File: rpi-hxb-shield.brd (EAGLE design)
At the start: 20 x 35 mm, 30 parts, among them Q1 CRYSTALX22, U2 24LC128-I/SN

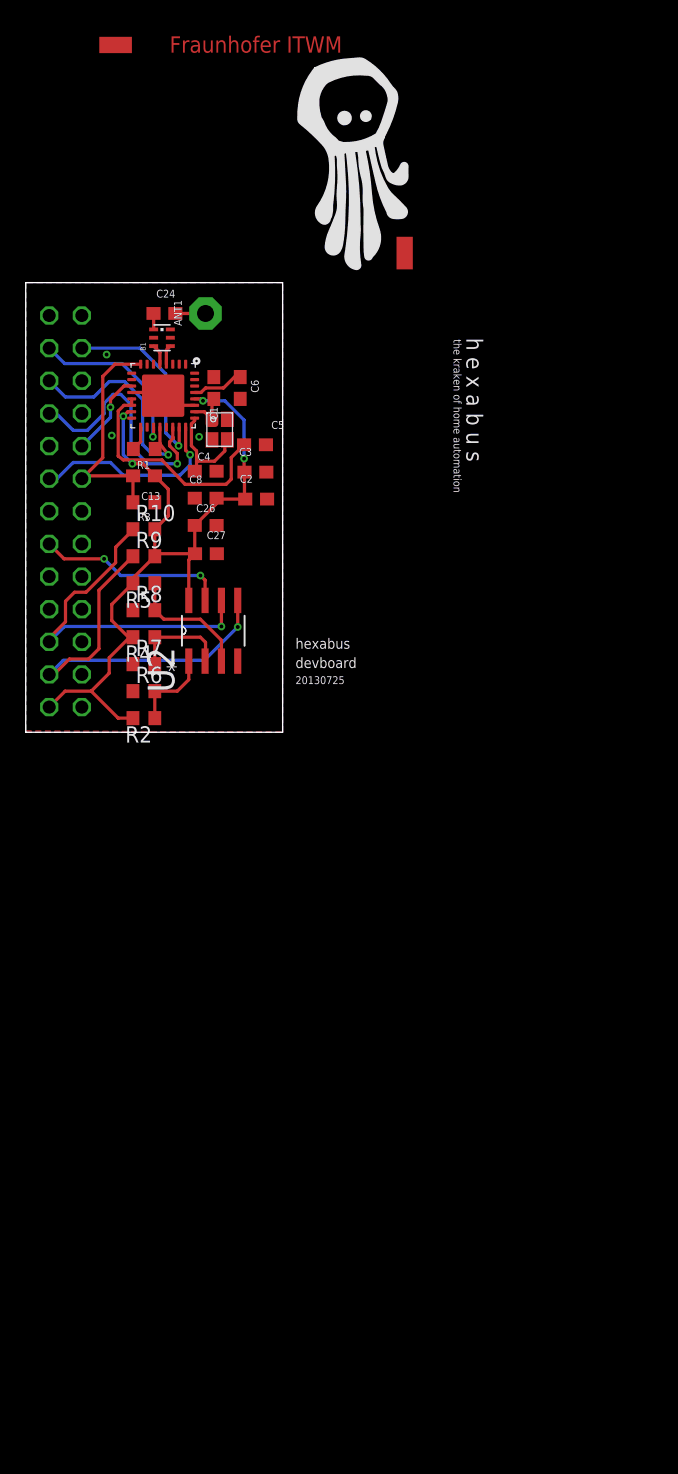
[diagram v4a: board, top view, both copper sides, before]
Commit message: sketch of new layout for accomodation the antenna on the pcb
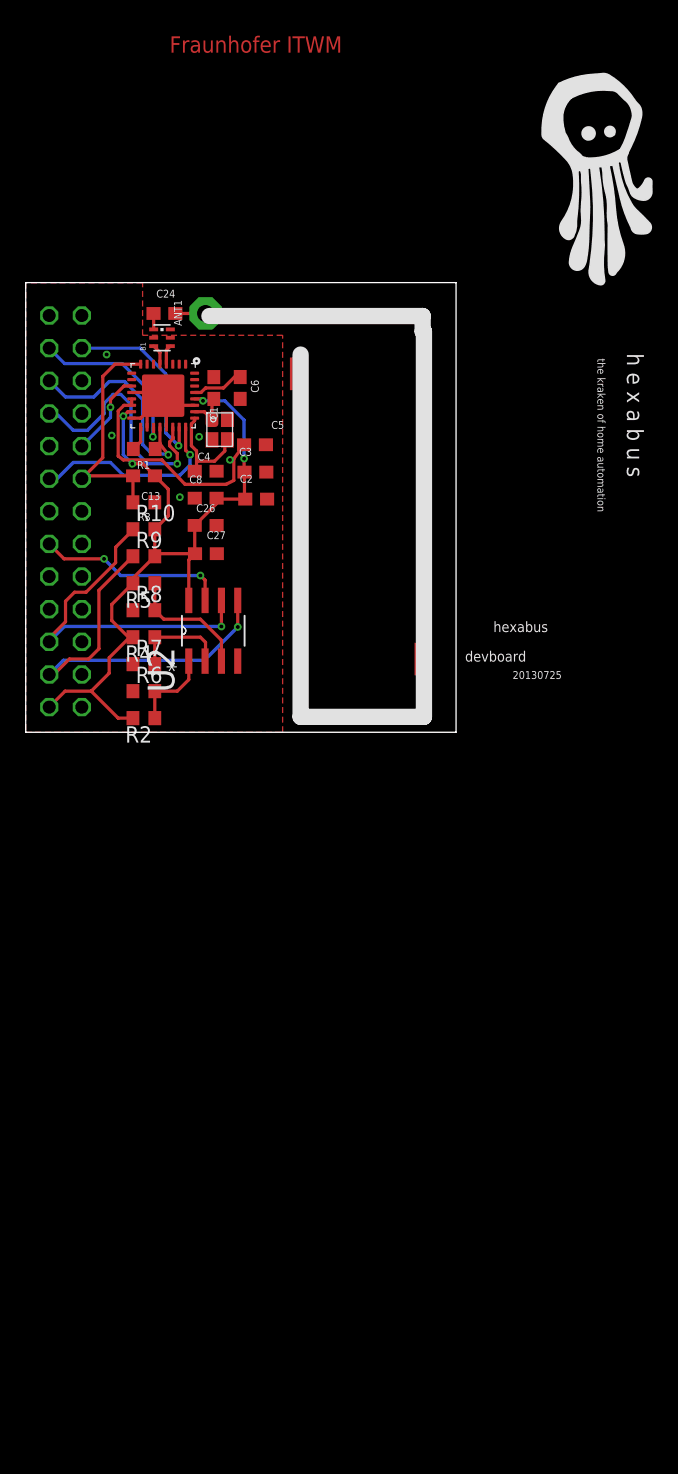
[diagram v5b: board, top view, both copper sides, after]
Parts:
- moved PAD2 31.6 mm to (30.9, 5.70)
- moved PAD1 29.3 mm to (21.2, 27.9), turned to 180 degrees
- moved U$1 19.0 mm to (40.2, 34.9)
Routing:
- net GND: track 5.31 -> 11.7 mm, vias 3 -> 5
- removed copper zone on layer 16, net GND
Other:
- board size 20 x 35 mm -> 33.5 x 35 mm
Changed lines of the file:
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@@
 <layer number="23" name="tOrigins" color="15" fill="1" visible="yes" active="yes"/>
 <layer number="24" name="bOrigins" color="15" fill="1" visible="yes" active="yes"/>
-<layer number="25" name="tNames" color="7" fill="1" visible="yes" active="yes"/>
+<layer number="25" name="tNames" color="7" fill="1" visible="no" active="yes"/>
 <layer number="26" name="bNames" color="7" fill="1" visible="yes" active="yes"/>
-<layer number="27" name="tValues" color="7" fill="1" visible="yes" active="yes"/>
+<layer number="27" name="tValues" color="7" fill="1" visible="no" active="yes"/>
 <layer number="28" name="bValues" color="7" fill="1" visible="yes" active="yes"/>
 <layer number="29" name="tStop" color="7" fill="3" visible="no" active="yes"/>
@@
 <board>
 <plain>
-<wire x1="0" y1="0" x2="20" y2="0" width="0" layer="20"/>
-<wire x1="20" y1="0" x2="20" y2="35" width="0" layer="20"/>
-<wire x1="20" y1="35" x2="0" y2="35" width="0" layer="20"/>
+<wire x1="0" y1="0" x2="33.5" y2="0" width="0" layer="20"/>
+<wire x1="33.5" y1="0" x2="33.5" y2="35" width="0" layer="20"/>
+<wire x1="33.5" y1="35" x2="0" y2="35" width="0" layer="20"/>
 <wire x1="0" y1="35" x2="0" y2="0" width="0" layer="20"/>
-<text x="34.3" y="30.7" size="1.27" layer="21" font="vector" ratio="15" rot="SR270">h e x a b u s</text>
+<text x="46.8" y="29.5" size="1.27" layer="21" font="vector" ratio="15" rot="SR270">h e x a b u s</text>
 <text x="11.2" y="52.9" size="1.27" layer="1" font="vector" ratio="12">Fraunhofer ITWM</text>
-<text x="33.3" y="30.6" size="0.6096" layer="21" font="vector" distance="100" rot="SR270">the kraken of home automation</text>
-<text x="21" y="6.5" size="0.8128" layer="21" font="vector" ratio="12">hexabus</text>
-<text x="21" y="5" size="0.8128" layer="21" font="vector">devboard</text>
-<text x="21" y="3.75" size="0.6096" layer="21" font="vector">20130725</text>
+<text x="44.5" y="29.1" size="0.6096" layer="21" font="vector" distance="100" rot="SR270">the kraken of home automation</text>
+<text x="36.4" y="7.8" size="0.8128" layer="21" font="vector" ratio="12">hexabus</text>
+<text x="34.2" y="5.5" size="0.8128" layer="21" font="vector">devboard</text>
+<text x="37.9" y="4.15" size="0.6096" layer="21" font="vector">20130725</text>
+<wire x1="14.3" y1="32.4" x2="30.9" y2="32.4" width="1.27" layer="21"/>
+<wire x1="30.9" y1="32.4" x2="30.9" y2="31.2" width="1.27" layer="21"/>
+<wire x1="30.9" y1="31.2" x2="31" y2="31.2" width="1.27" layer="21"/>
+<wire x1="31" y1="31.2" x2="31" y2="1.2" width="1.27" layer="21"/>
+<wire x1="31" y1="1.2" x2="21.4" y2="1.2" width="1.27" layer="21"/>
+<wire x1="21.4" y1="1.2" x2="21.4" y2="29.4" width="1.27" layer="21"/>
 </plain>
 <attributes>
@@
 <attribute name="NAME" x="13.375" y="21.155" size="0.6096" layer="25"/>
 </element>
-<element name="PAD1" library="wirepad" package="SMD1,27-2,54" value="" x="7" y="53.5" smashed="yes" rot="R90">
-<attribute name="VALUE" x="7" y="53.5" size="0.0254" layer="27" rot="R90"/>
-</element>
-<element name="PAD2" library="wirepad" package="SMD1,27-2,54" value="" x="29.5" y="37.3" smashed="yes">
-<attribute name="VALUE" x="29.5" y="37.3" size="0.0254" layer="27"/>
-</element>
-<element name="U$1" library="artwork" package="HEXAKRAKE" value="HEXAKRAKE" x="21.2" y="36.1"/>
+<element name="PAD1" library="wirepad" package="SMD1,27-2,54" value="" x="21.2" y="27.9" smashed="yes" rot="R180">
+<attribute name="VALUE" x="21.2" y="27.9" size="0.0254" layer="27" rot="R180"/>
+</element>
+<element name="PAD2" library="wirepad" package="SMD1,27-2,54" value="" x="30.9" y="5.7" smashed="yes">
+<attribute name="VALUE" x="30.9" y="5.7" size="0.0254" layer="27"/>
+</element>
+<element name="U$1" library="artwork" package="HEXAKRAKE" value="HEXAKRAKE" x="40.2" y="34.9"/>
 <element name="U2" library="hexabus" package="SOIC127P600X175-8N" value="24LC128-I/SN" x="14.6" y="7.9" rot="R90">
 <attribute name="PACKAGE" value="SOIC-8" x="14.6" y="7.9" size="1.778" layer="27" rot="R90" display="off"/>
@@
 <contactref element="JP1" pad="14"/>
 <contactref element="JP1" pad="20"/>
-<polygon width="0.254" layer="16" spacing="0.254">
-<vertex x="0" y="0"/>
-<vertex x="20" y="0"/>
-<vertex x="20" y="35"/>
-<vertex x="0" y="35"/>
-</polygon>
-<polygon width="0.254" layer="1" spacing="0.254">
-<vertex x="0" y="0.1"/>
-<vertex x="20" y="0"/>
-<vertex x="20" y="35"/>
-<vertex x="0" y="35"/>
-</polygon>
 <via x="6.7" y="23.1" extent="1-16" drill="0.3"/>
 <via x="6.3" y="29.4" extent="1-16" drill="0.3"/>
 <wire x1="8.25" y1="26.45" x2="10.45" y2="26.45" width="0.254" layer="1"/>
 <wire x1="10.45" y1="26.45" x2="10.7" y2="26.2" width="0.254" layer="1"/>
-<wire x1="13.15" y1="25.45" x2="11.45" y2="25.45" width="0.254" layer="1"/>
-<wire x1="11.45" y1="25.45" x2="10.7" y2="26.2" width="0.254" layer="1"/>
 <via x="13.5" y="23" extent="1-16" drill="0.3"/>
-<wire x1="14.5" y1="22.76" x2="14.86" y2="20.32" width="0" layer="19" extent="1-1"/>
+<wire x1="8.25" y1="24.45" x2="8.95" y2="24.45" width="0.254" layer="1"/>
+<wire x1="8.95" y1="24.45" x2="9.45" y2="24.95" width="0.254" layer="1"/>
+<wire x1="9.45" y1="23.75" x2="9.45" y2="24.95" width="0.254" layer="1"/>
+<wire x1="9.45" y1="24.95" x2="10.7" y2="26.2" width="0.254" layer="1"/>
+<wire x1="10.95" y1="23.75" x2="10.95" y2="25.6" width="0.254" layer="1"/>
+<wire x1="10.95" y1="25.6" x2="10.95" y2="25.95" width="0.254" layer="1"/>
+<wire x1="10.95" y1="25.95" x2="10.7" y2="26.2" width="0.254" layer="1"/>
+<via x="15.9" y="21.2" extent="1-16" drill="0.3"/>
+<via x="12" y="18.3" extent="1-16" drill="0.3"/>
+<wire x1="13.15" y1="25.45" x2="11.1" y2="25.45" width="0.254" layer="1"/>
+<wire x1="11.1" y1="25.45" x2="10.95" y2="25.6" width="0.254" layer="1"/>
+<polygon width="0.254" layer="1">
+<vertex x="0" y="0"/>
+<vertex x="20" y="0"/>
+<vertex x="20" y="30.9"/>
+<vertex x="9.1" y="30.9"/>
+<vertex x="9.1" y="35"/>
+<vertex x="0" y="35"/>
+</polygon>
+<wire x1="11.2602" y1="30.7086" x2="11.2602" y2="31.3586" width="0" layer="19" extent="1-1"/>
 <wire x1="13.15" y1="25.45" x2="13.15" y2="26.95" width="0" layer="19" extent="1-1"/>
-<wire x1="10.95" y1="23.75" x2="11.45" y2="25.45" width="0" layer="19" extent="1-1"/>
-<wire x1="9.45" y1="23.75" x2="10.95" y2="23.75" width="0" layer="19" extent="1-1"/>
-<wire x1="8.25" y1="24.45" x2="9.45" y2="23.75" width="0" layer="19" extent="1-1"/>
+<wire x1="12" y1="18.3" x2="10.05" y2="17.9" width="0" layer="19" extent="1-1"/>
+<wire x1="14.5" y1="22.76" x2="15.7" y2="24.36" width="0" layer="19" extent="1-1"/>
 <wire x1="6.7" y1="23.1" x2="8.25" y2="24.45" width="0" layer="19" extent="1-1"/>
-<wire x1="13.16" y1="18.22" x2="14.86" y2="20.32" width="0" layer="19" extent="1-1"/>
+<wire x1="15.9" y1="21.2" x2="14.5" y2="22.76" width="0" layer="19" extent="1-1"/>
 </signal>
 <signal name="IRQ">
@@
 <wire x1="10.6" y1="21.2" x2="12.4" y2="19.3" width="0.254" layer="1"/>
 <wire x1="12.4" y1="19.3" x2="15.6" y2="19.3" width="0.254" layer="1"/>
-<wire x1="15.6" y1="19.3" x2="16" y2="19.7" width="0.254" layer="1"/>
-<wire x1="16" y1="19.7" x2="16" y2="21.38" width="0.254" layer="1"/>
-<wire x1="16" y1="21.38" x2="17" y2="22.38" width="0.254" layer="1"/>
+<wire x1="15.6" y1="19.3" x2="16.2" y2="19.6" width="0.254" layer="1"/>
+<wire x1="16.2" y1="19.6" x2="16.2" y2="21.28" width="0.254" layer="1"/>
+<wire x1="16.2" y1="21.28" x2="17" y2="22.38" width="0.254" layer="1"/>
 <wire x1="8.25" y1="25.45" x2="8.25" y2="25.95" width="0.254" layer="1"/>
 </signal>

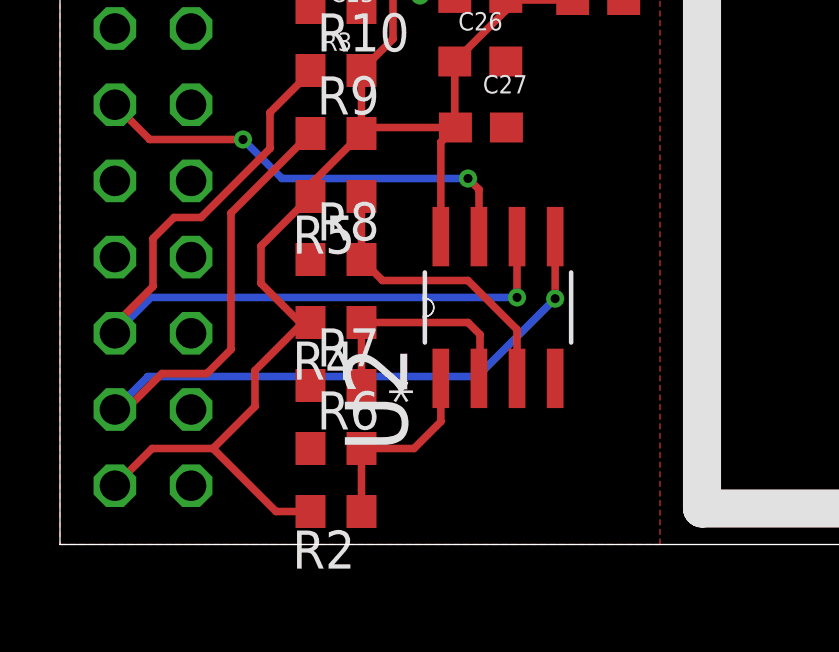
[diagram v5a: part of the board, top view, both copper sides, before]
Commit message: EEPOM now with fixed address (hardwired)
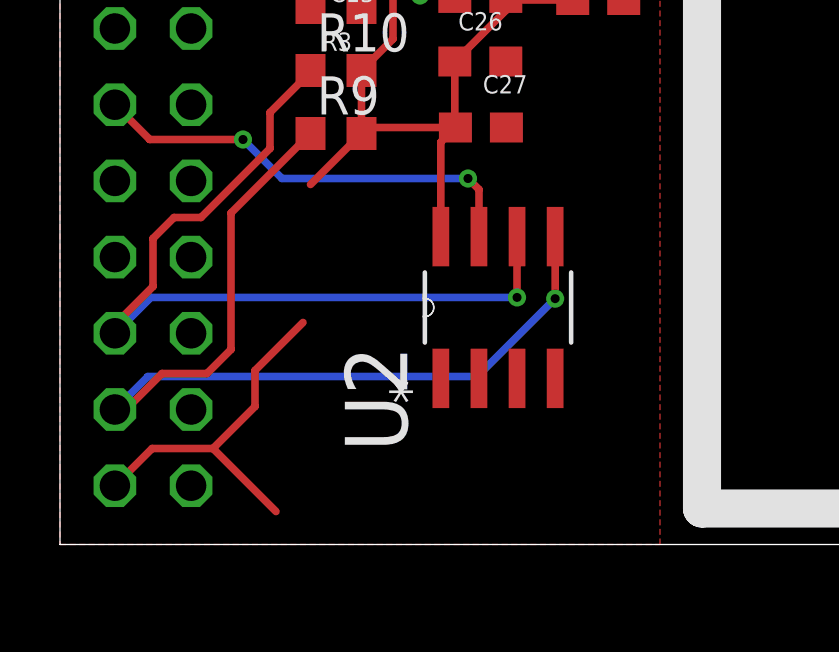
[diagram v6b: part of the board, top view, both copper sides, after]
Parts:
- removed R2, R4, R5, R6, R7, R8: 0R, rcl:R0603
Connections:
- removed net N$10: R5.1, R8.2, U2.3
- removed net N$4: R2.1, R6.2, U2.1
- removed net N$9: R4.1, R7.2, U2.2
- net GND: now also U2.1, U2.2, U2.3; no longer R6.1, R7.1, R8.1
- net VCC: no longer R2.2, R4.2, R5.2
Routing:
- net N$10: track 9.88 -> 0.00 mm
- net N$9: track 7.69 -> 0.00 mm
- net VCC: track 61.3 -> 53.7 mm
- net N$4: track 6.56 -> 0.00 mm
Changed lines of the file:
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@@
 <attribute name="OC_FARNELL" value="9757937" x="14.6" y="7.9" size="1.778" layer="27" rot="R90" display="off"/>
 </element>
-<element name="R2" library="rcl" package="R0603" value="0R" x="9.2" y="1.1" rot="R180"/>
-<element name="R4" library="rcl" package="R0603" value="0R" x="9.2" y="7.4" rot="R180"/>
-<element name="R5" library="rcl" package="R0603" value="0R" x="9.2" y="11.6" rot="R180"/>
-<element name="R6" library="rcl" package="R0603" value="0R" x="9.2" y="3.2"/>
-<element name="R7" library="rcl" package="R0603" value="0R" x="9.2" y="5.3"/>
-<element name="R8" library="rcl" package="R0603" value="0R" x="9.2" y="9.5"/>
 <element name="JP1" library="pinhead" package="2X13" value="" x="3.1" y="17.2" rot="MR90"/>
 <element name="R9" library="rcl" package="R0603" value="4k7" x="9.2" y="13.7"/>
@@
 <contactref element="U1" pad="33"/>
 <contactref element="U2" pad="4"/>
-<contactref element="R8" pad="1"/>
-<contactref element="R7" pad="1"/>
-<contactref element="R6" pad="1"/>
 <contactref element="JP1" pad="25"/>
 <contactref element="JP1" pad="9"/>
@@
 <vertex x="0" y="35"/>
 </polygon>
+<contactref element="U2" pad="3"/>
+<contactref element="U2" pad="2"/>
+<contactref element="U2" pad="1"/>
 <wire x1="11.2602" y1="30.7086" x2="11.2602" y2="31.3586" width="0" layer="19" extent="1-1"/>
+<wire x1="15.235" y1="5.5378" x2="16.505" y2="5.5378" width="0" layer="19" extent="1-1"/>
+<wire x1="13.965" y1="5.5378" x2="15.235" y2="5.5378" width="0" layer="19" extent="1-1"/>
+<wire x1="12.695" y1="5.5378" x2="13.965" y2="5.5378" width="0" layer="19" extent="1-1"/>
 <wire x1="13.15" y1="25.45" x2="13.15" y2="26.95" width="0" layer="19" extent="1-1"/>
 <wire x1="12" y1="18.3" x2="10.05" y2="17.9" width="0" layer="19" extent="1-1"/>
@@
 <contactref element="U2" pad="8"/>
 <contactref element="U2" pad="8"/>
-<contactref element="R5" pad="2"/>
-<contactref element="R4" pad="2"/>
-<contactref element="R2" pad="2"/>
 <contactref element="JP1" pad="1"/>
 <contactref element="R9" pad="2"/>
@@
 <wire x1="1.83" y1="1.96" x2="3.07" y2="3.2" width="0.254" layer="1"/>
 <wire x1="3.07" y1="3.2" x2="5.1" y2="3.2" width="0.254" layer="1"/>
-<wire x1="8.35" y1="1.1" x2="7.2" y2="1.1" width="0.254" layer="1"/>
 <wire x1="7.2" y1="1.1" x2="5.1" y2="3.2" width="0.254" layer="1"/>
 <wire x1="13.18" y1="13.9" x2="12.695" y2="13.415" width="0.254" layer="1"/>
@@
 <wire x1="11.1" y1="16.85" x2="11.1" y2="18.92" width="0.254" layer="1"/>
 <wire x1="11.1" y1="18.92" x2="10.06" y2="19.96" width="0.254" layer="1"/>
-<wire x1="8.35" y1="7.4" x2="8.1" y2="7.4" width="0.254" layer="1"/>
 <wire x1="8.1" y1="7.4" x2="6.5" y2="5.8" width="0.254" layer="1"/>
 <wire x1="6.5" y1="5.8" x2="6.5" y2="4.6" width="0.254" layer="1"/>
 <wire x1="6.5" y1="4.6" x2="5.1" y2="3.2" width="0.254" layer="1"/>
-<wire x1="8.35" y1="7.4" x2="8" y2="7.4" width="0.254" layer="1"/>
-<wire x1="8" y1="7.4" x2="6.7" y2="8.7" width="0.254" layer="1"/>
-<wire x1="6.7" y1="8.7" x2="6.7" y2="9.95" width="0.254" layer="1"/>
-<wire x1="6.7" y1="9.95" x2="8.35" y2="11.6" width="0.254" layer="1"/>
-<wire x1="8.35" y1="11.6" x2="8.35" y2="12" width="0.254" layer="1"/>
 <wire x1="8.35" y1="12" x2="10.05" y2="13.7" width="0.254" layer="1"/>
 <wire x1="13.15" y1="25.95" x2="13.65" y2="25.95" width="0.254" layer="1"/>
@@
 <wire x1="8.3" y1="20.9" x2="9.12" y2="20.9" width="0.254" layer="1"/>
 <wire x1="9.12" y1="20.9" x2="10.06" y2="19.96" width="0.254" layer="1"/>
+<wire x1="8.1" y1="7.4" x2="8.35" y2="12" width="0" layer="19" extent="1-1"/>
 </signal>
 <signal name="SDA">
@@
 <wire x1="3.025" y1="8.235" x2="1.83" y2="7.04" width="0.254" layer="16"/>
 </signal>
-<signal name="N$4">
-<contactref element="U2" pad="1"/>
-<contactref element="R2" pad="1"/>
-<contactref element="R6" pad="2"/>
-<wire x1="10.05" y1="1.1" x2="10.05" y2="3.2" width="0.254" layer="1"/>
-<wire x1="12.695" y1="5.5378" x2="12.695" y2="4.095" width="0.254" layer="1"/>
-<wire x1="12.695" y1="4.095" x2="11.8" y2="3.2" width="0.254" layer="1"/>
-<wire x1="11.8" y1="3.2" x2="10.05" y2="3.2" width="0.254" layer="1"/>
-</signal>
-<signal name="N$9">
-<contactref element="U2" pad="2"/>
-<contactref element="R4" pad="1"/>
-<contactref element="R7" pad="2"/>
-<wire x1="10.05" y1="7.4" x2="13.6" y2="7.4" width="0.254" layer="1"/>
-<wire x1="13.6" y1="7.4" x2="14" y2="7" width="0.254" layer="1"/>
-<wire x1="14" y1="7" x2="14" y2="5.5728" width="0.254" layer="1"/>
-<wire x1="14" y1="5.5728" x2="13.965" y2="5.5378" width="0.254" layer="1"/>
-<wire x1="10.05" y1="5.3" x2="10.05" y2="7.4" width="0.254" layer="1"/>
-</signal>
-<signal name="N$10">
-<contactref element="U2" pad="3"/>
-<contactref element="R5" pad="1"/>
-<contactref element="R8" pad="2"/>
-<wire x1="15.235" y1="5.5378" x2="15.235" y2="7.165" width="0.254" layer="1"/>
-<wire x1="10.05" y1="9.5" x2="10.75" y2="8.8" width="0.254" layer="1"/>
-<wire x1="10.75" y1="8.8" x2="13.6" y2="8.8" width="0.254" layer="1"/>
-<wire x1="13.6" y1="8.8" x2="15.235" y2="7.165" width="0.254" layer="1"/>
-<wire x1="10.05" y1="9.5" x2="10.05" y2="11.6" width="0.254" layer="1"/>
-</signal>
 <signal name="WP">

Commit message: routing
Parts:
- moved U$1 30.2 mm to (22.0, 10.8)
- moved C3 11.2 mm to (9.40, 13.0), turned to 180 degrees
- moved C5 6.00 mm to (14.5, 17.4)
- moved C26 5.32 mm to (14.5, 10.8)
- moved C27 5.32 mm to (14.5, 8.60)
- moved C8 5.24 mm to (14.5, 13.0), turned to 0 degrees
- moved R9 5.10 mm to (9.40, 8.60)
- moved R10 5.00 mm to (9.40, 10.8)
- moved C2 4.53 mm to (14.5, 15.2)
- moved U2 3.90 mm to (14.5, 4.00)
- moved R3 2.71 mm to (9.40, 15.2)
- moved C13 2.57 mm to (9.40, 17.4)
- moved R1 2.46 mm to (9.40, 19.6)
- moved PAD1 1.12 mm to (21.0, 26.8)
- moved C4 0.87 mm to (14.5, 19.6)
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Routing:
- net SDA: track 31.3 -> 25.9 mm
- net WP: track 14.9 -> 20.2 mm, vias 2 -> 0
- net SCL: track 27.9 -> 24.6 mm
- net VCC: track 53.7 -> 57.0 mm, vias 4 -> 5
- net N$5: track 1.94 -> 4.55 mm
- net N$2: track 18.3 -> 15.7 mm
- net GND: track 11.7 -> 13.6 mm
- net AT_RST: track 18.1 -> 20.0 mm
- net N$31: track 7.93 -> 9.47 mm
- net MISO: track 17.0 -> 15.5 mm
- net N$1: track 4.05 -> 4.55 mm
- added copper zone on layer 16, net GND
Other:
- board text added: "20140206"
- board text added: "rpi-shield"
- board text removed: "20130725"
- board text removed: "devboard"
